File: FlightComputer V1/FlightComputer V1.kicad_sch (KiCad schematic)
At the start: 0 parts

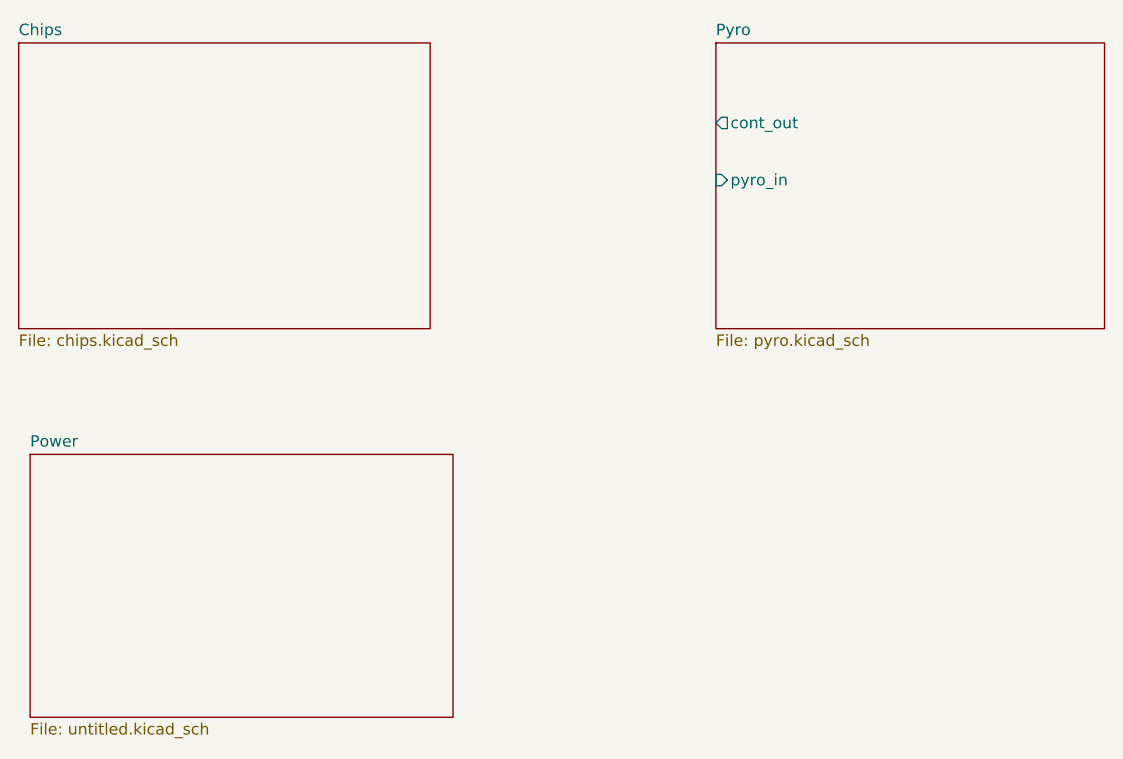
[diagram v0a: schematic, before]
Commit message: Added power circuitry
reset button, ADC for voltage detection, voltage regulator and switch for total power on and off. Screw terminal to interface between battery pack and PCB.
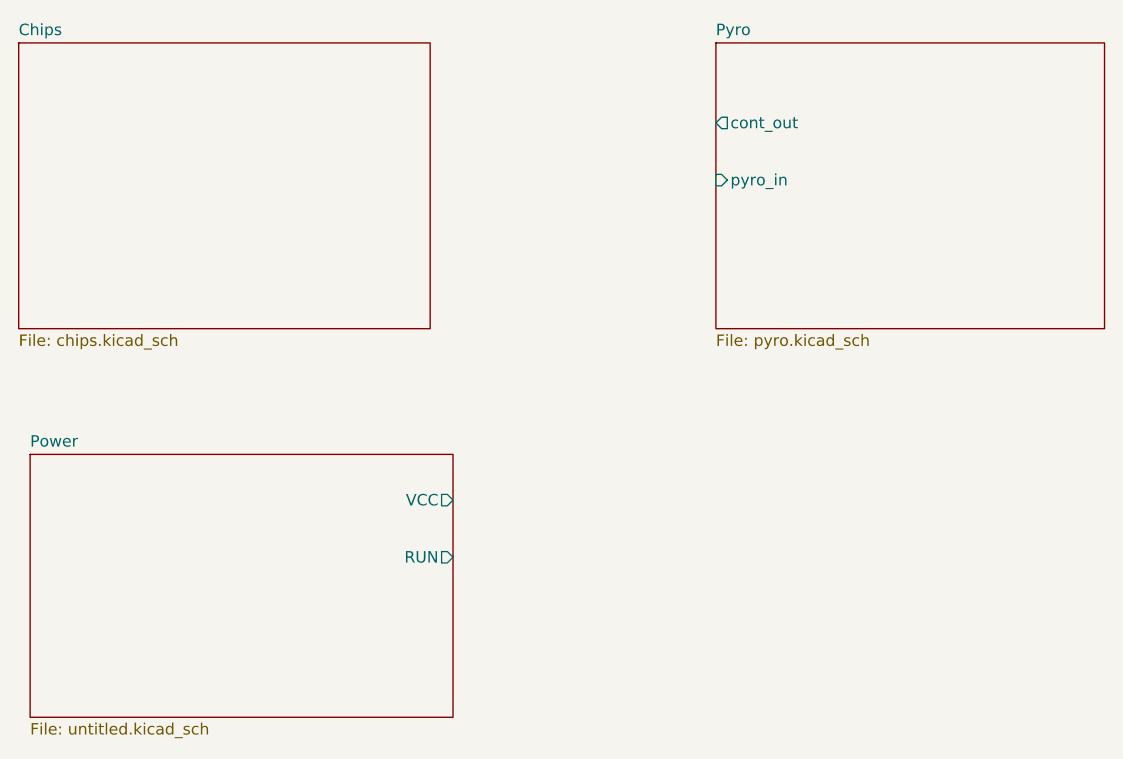
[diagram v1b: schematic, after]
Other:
- sheet Power ports: added RUN, VCC; removed none
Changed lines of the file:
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@@
+			)
+		)
+		(pin "VCC" output
+			(at 135.89 120.65 0)
+			(effects
+				(font
+					(size 1.27 1.27)
+				)
+				(justify right)
+			)
+		)
+		(pin "RUN" output
+			(at 135.89 127 0)
+			(effects
+				(font
+					(size 1.27 1.27)
+				)
+				(justify right)
 			)
 		)
